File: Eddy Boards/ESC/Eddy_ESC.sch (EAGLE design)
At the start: 10 parts

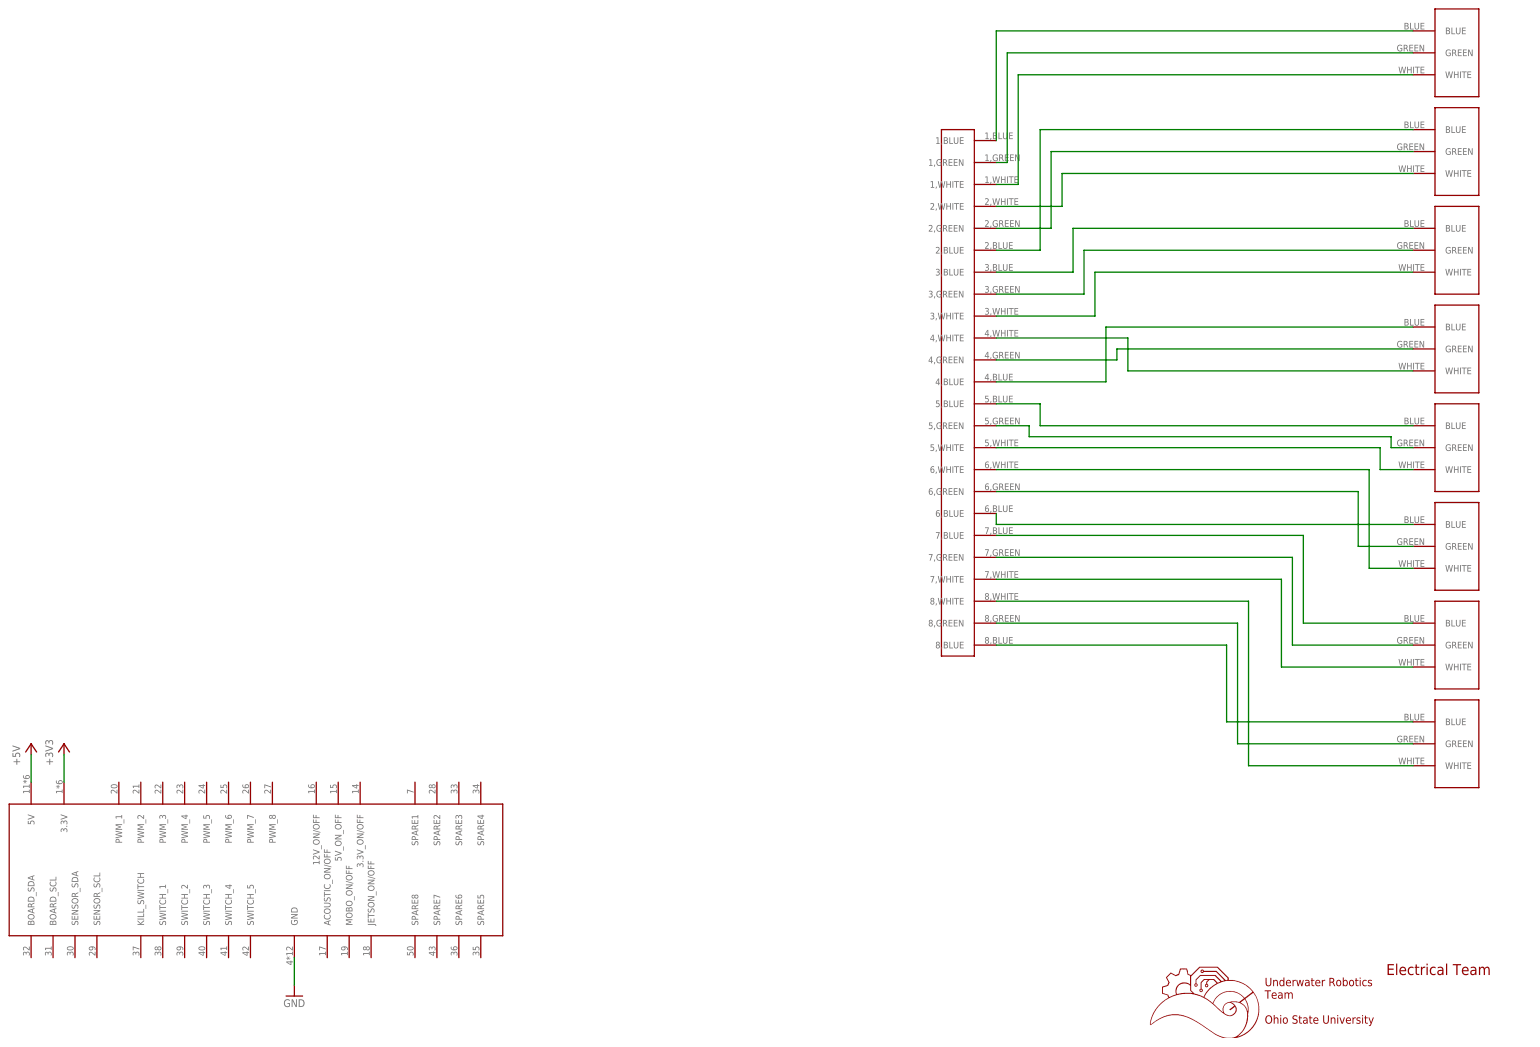
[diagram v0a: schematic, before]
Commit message: addded PWM's to connector and adjusted positioning
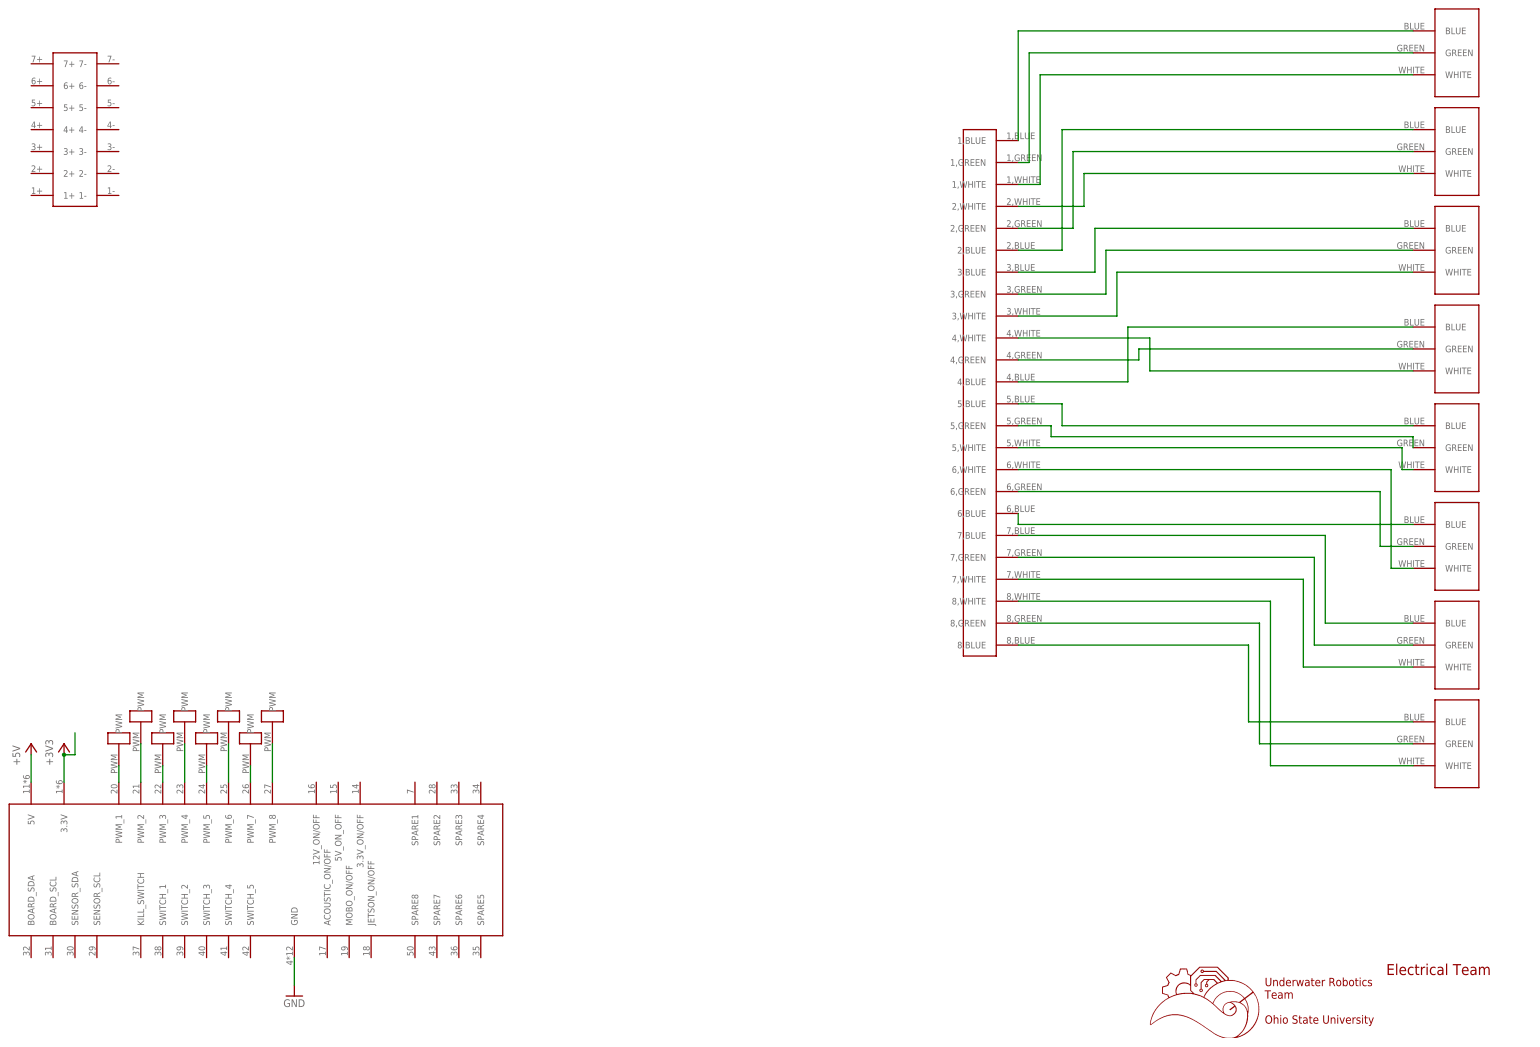
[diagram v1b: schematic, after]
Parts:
- added U$11: 14PIN_VERT, 14_Pin_Connector_Vert:14PIN_VERT
- added U$12, U$13, U$14, U$15, U$16, U$17, U$18, U$19: MALE1PINHEADER, Male_Header_1Pin:MALE1PINHEADER
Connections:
- new net N$25: U$1.PWM_1, U$12.PWM
- new net N$26: U$1.PWM_2, U$13.PWM
- new net N$27: U$1.PWM_3, U$14.PWM
- new net N$28: U$1.PWM_4, U$16.PWM
- new net N$29: U$1.PWM_5, U$15.PWM
- new net N$30: U$1.PWM_6, U$17.PWM
- new net N$31: U$1.PWM_7, U$18.PWM
- new net N$32: U$1.PWM_8, U$19.PWM

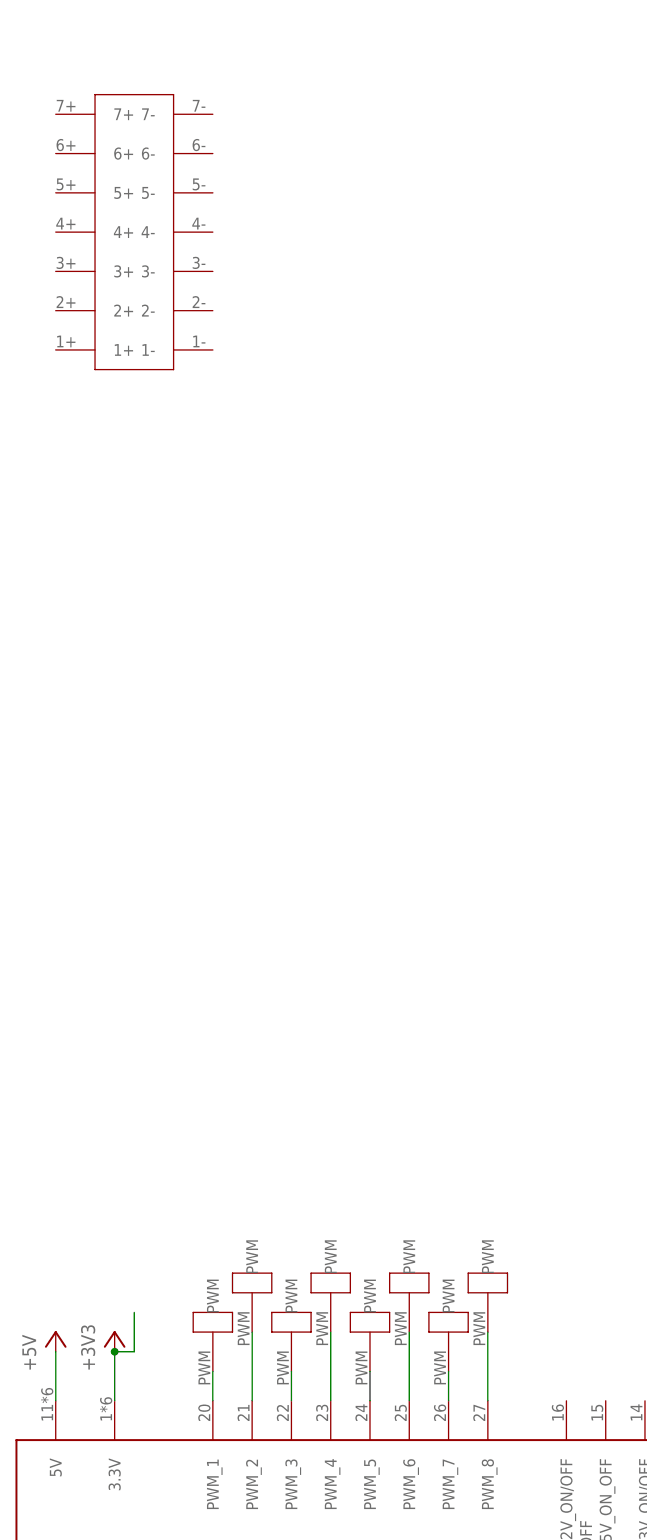
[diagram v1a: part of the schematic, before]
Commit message: added LED
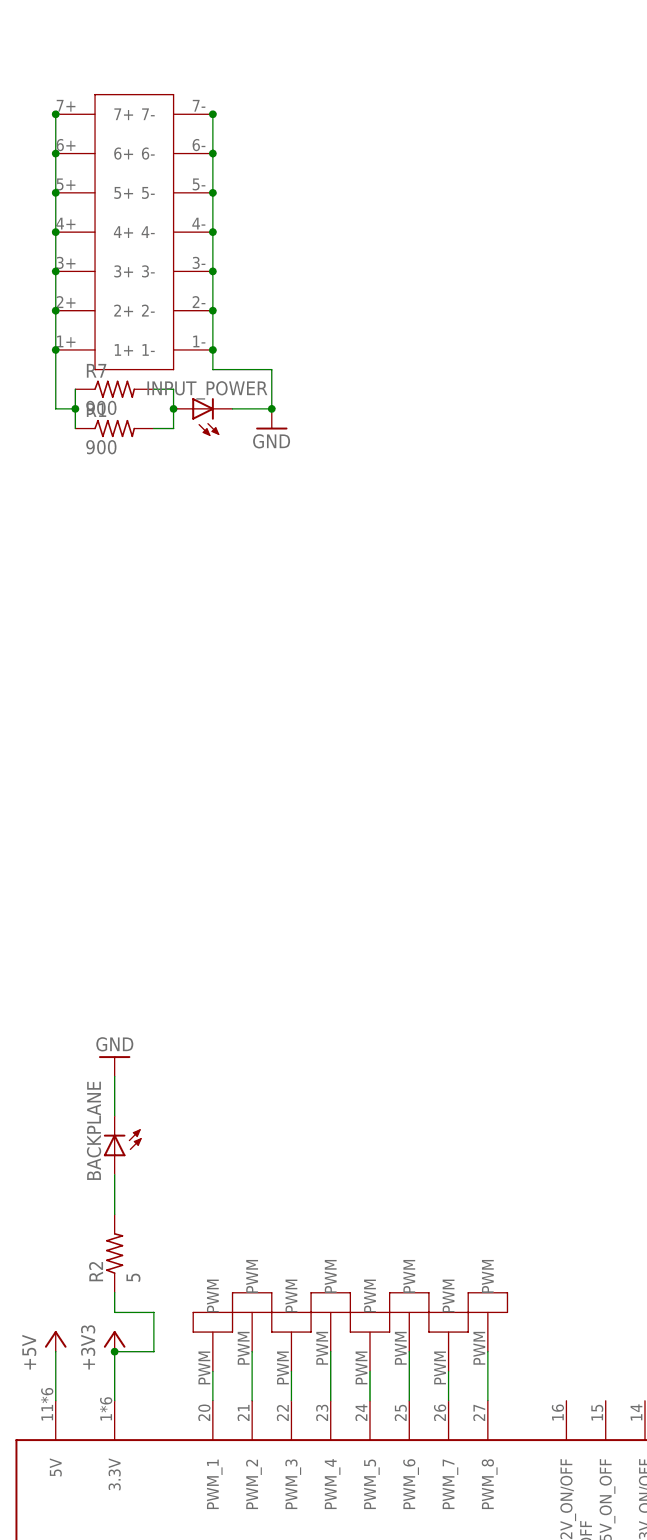
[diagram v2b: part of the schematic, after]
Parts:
- added BACKPLANE, INPUT_POWER: (no value), led:LEDCHIPLED_0603
- added R1, R7: 900, resistor:R-US_R0603
- added R2: 5, resistor:R-US_R0603
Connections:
- new net N$33: INPUT_POWER.A, R1.2, R7.2
- new net N$34: BACKPLANE.A, R2.2
- new net N$39: R1.1, R7.1, U$11.1+, U$11.2+, U$11.3+, U$11.4+, U$11.5+, U$11.6+, U$11.7+
- new net N$44: U$11.3-
- net +3V3: now also R2.1
- net GND: now also BACKPLANE.C, INPUT_POWER.C, U$11.1-, U$11.2-, U$11.4-, U$11.5-, U$11.6-, U$11.7-

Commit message: finished sheet 1, moved items on board around- will add labels to sheet 1 later
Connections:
- new net N$35: U$1.BOARD_SDA
- new net N$36: U$1.BOARD_SCL

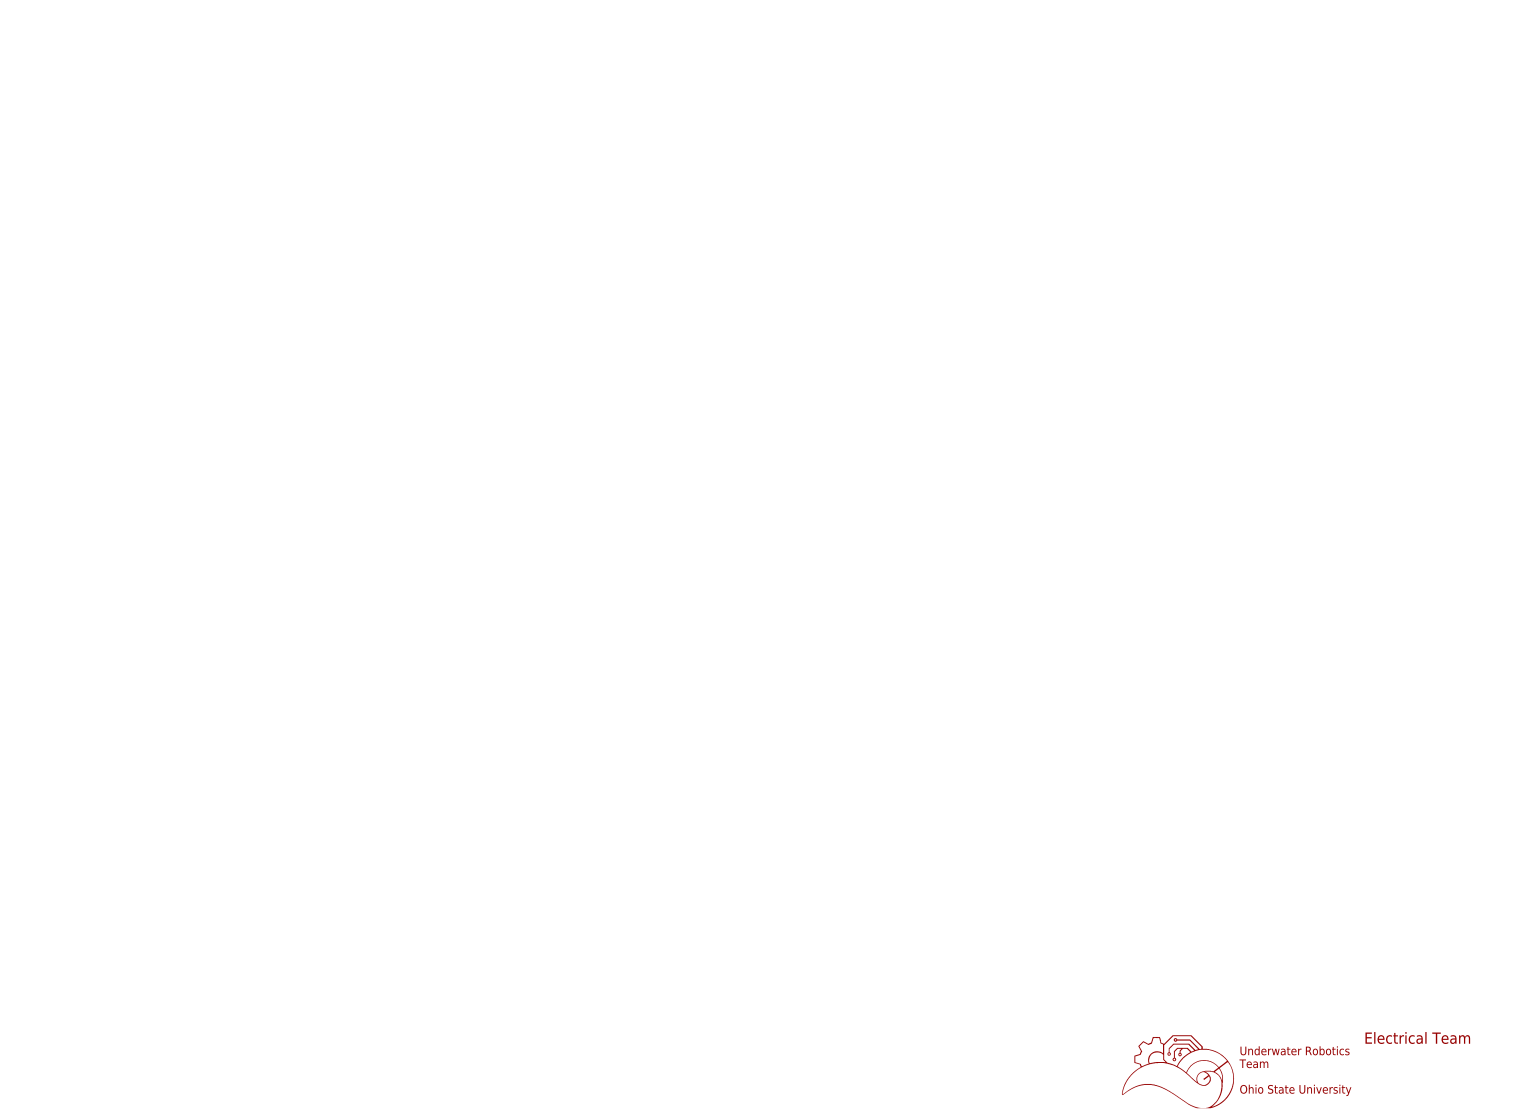
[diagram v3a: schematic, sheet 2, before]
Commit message: started sheet 2 of schematic, need explanation of esc's the alternating setup is confusing me. Need labels on sheet 1
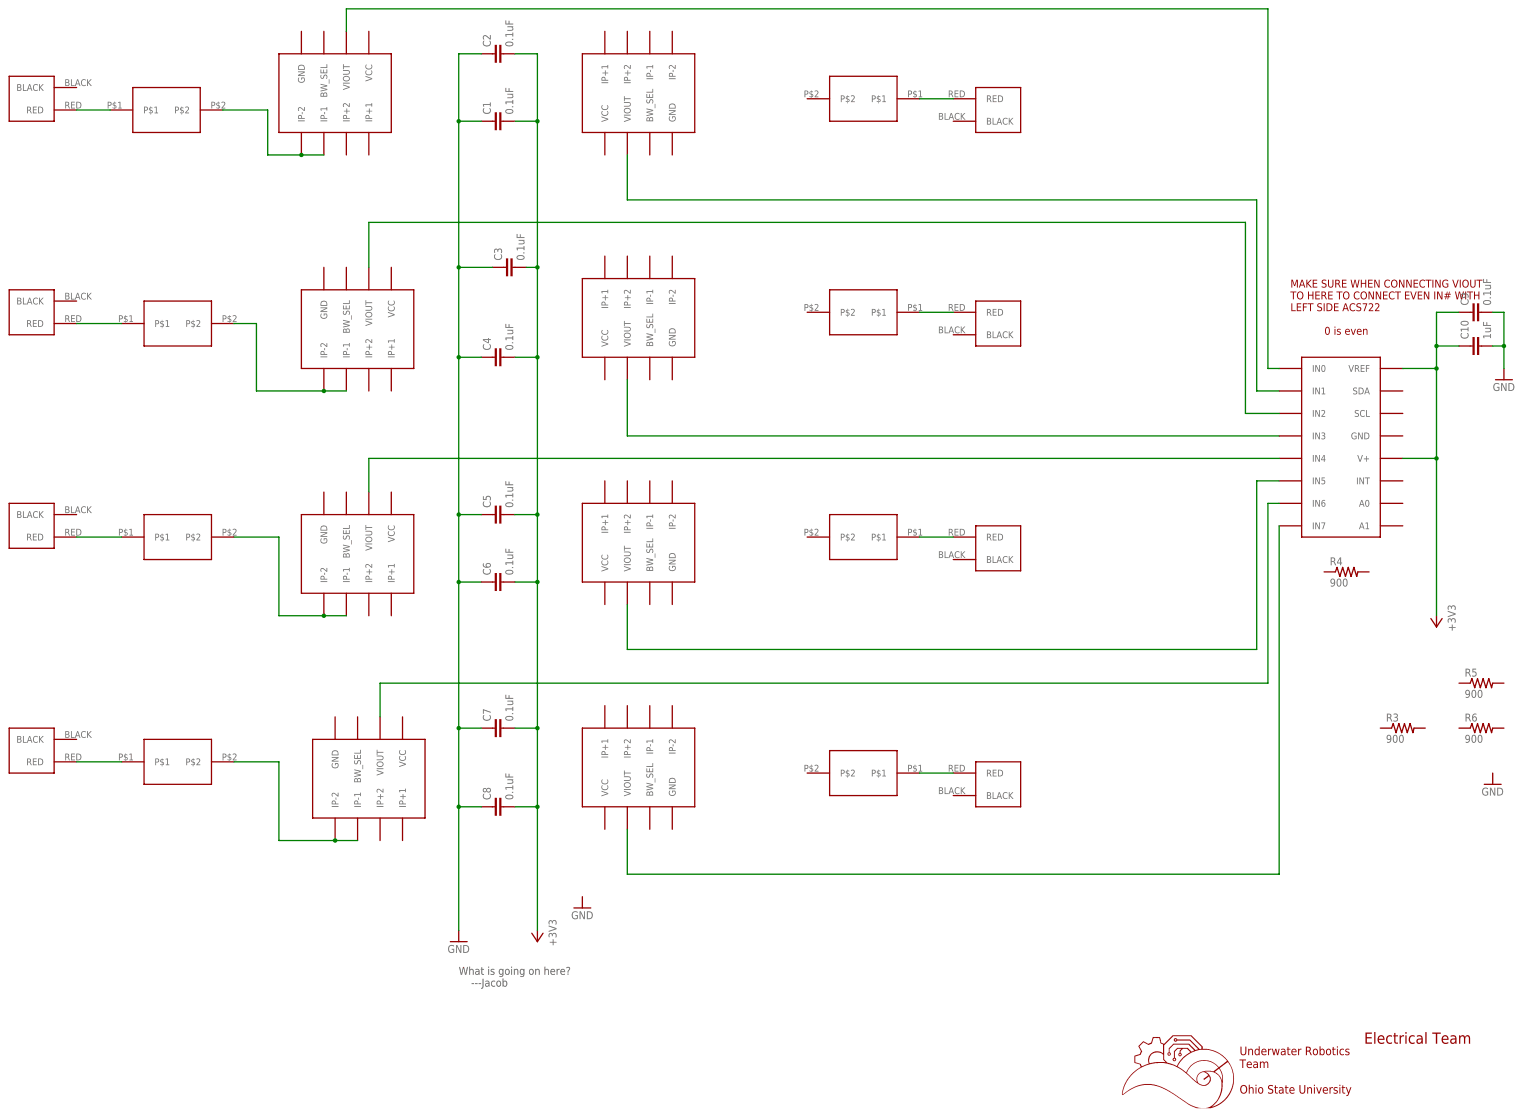
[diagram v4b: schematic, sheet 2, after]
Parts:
- added C1, C2, C3, C4, C5, C6, C7, C8, C9: 0.1uF, rcl:C-EUC0603
- added C10: 1uF, rcl:C-EUC0603
- added R3, R4, R5, R6: 900, resistor:R-US_R0603
- added U$20, U$21, U$22, U$23, U$24, U$25, U$26, U$27: 1711725, Screw_Terminals:1711725
- added U$28, U$29, U$30, U$31, U$32, U$33, U$34, U$35: ACS722, ACS722:ACS722
- added U$36: ADC128D818, ADC128D818:ADC128D818
- added U$37, U$38, U$39, U$40, U$41, U$42, U$43, U$44: 1206SFH, 1206SFH:1206SFH
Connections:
- new net N$37: U$34.VIOUT, U$36.IN4
- new net N$38: U$29.VIOUT, U$36.IN3
- new net N$40: U$33.IP-1, U$33.IP-2, U$38.P$2
- new net N$41: U$34.IP-1, U$34.IP-2, U$39.P$2
- new net N$42: U$31.VIOUT, U$36.IN7
- new net N$43: U$35.VIOUT, U$36.IN6
- new net N$45: U$30.VIOUT, U$36.IN5
- new net N$46: U$32.IP-1, U$32.IP-2, U$37.P$2
- new net N$47: U$35.IP-1, U$35.IP-2, U$40.P$2
- new net N$48: U$33.VIOUT, U$36.IN2
- new net N$49: U$28.VIOUT, U$36.IN1
- new net N$50: U$32.VIOUT, U$36.IN0
- new net N$51: U$24.RED, U$37.P$1
- new net N$52: U$25.RED, U$38.P$1
- new net N$53: U$26.RED, U$39.P$1
- new net N$54: U$27.RED, U$40.P$1
- new net N$55: U$20.RED, U$41.P$1
- new net N$56: U$21.RED, U$42.P$1
- new net N$57: U$22.RED, U$43.P$1
- new net N$58: U$23.RED, U$44.P$1
- net +3V3: now also C1.2, C10.1, C2.2, C3.2, C4.2, C5.2, C6.2, C7.2, C8.2, C9.1, U$36.V+, U$36.VREF
- net GND: now also C1.1, C10.2, C2.1, C3.1, C4.1, C5.1, C6.1, C7.1, C8.1, C9.2
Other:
- note added: "Big connector at bottom of board <----------"
- note added: "MAKE SURE WHEN CONNECTING VIOUT TO HERE TO CONNECT EVEN IN# WITH LEFT SIDE ACS722 0 is even"
- note added: "What is going on here? ---Jacob"
